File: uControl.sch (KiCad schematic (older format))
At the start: 4 parts

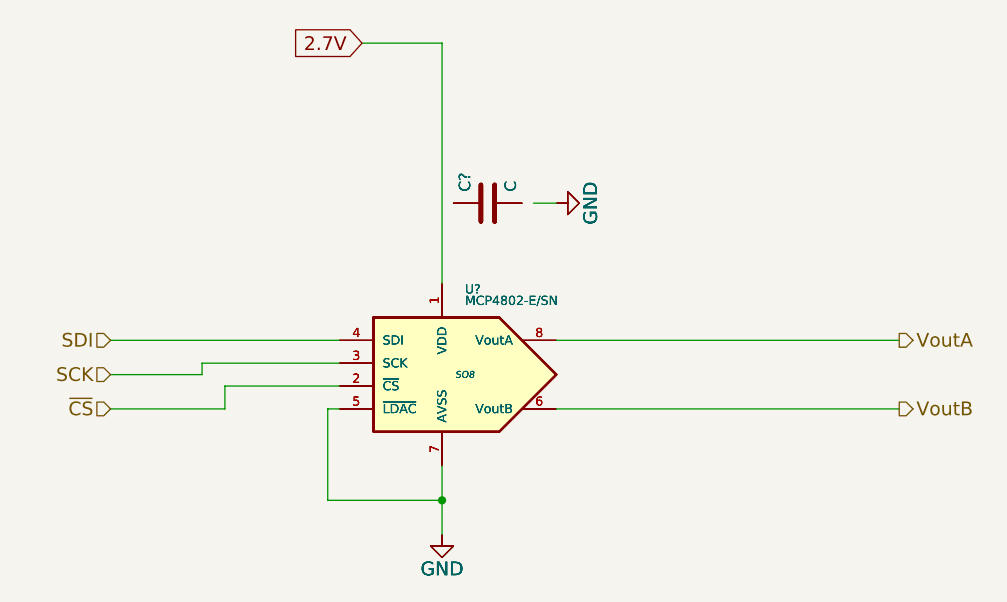
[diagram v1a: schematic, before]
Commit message: added additional regulator to power the ACS711 and potentially a micro at 3.3V
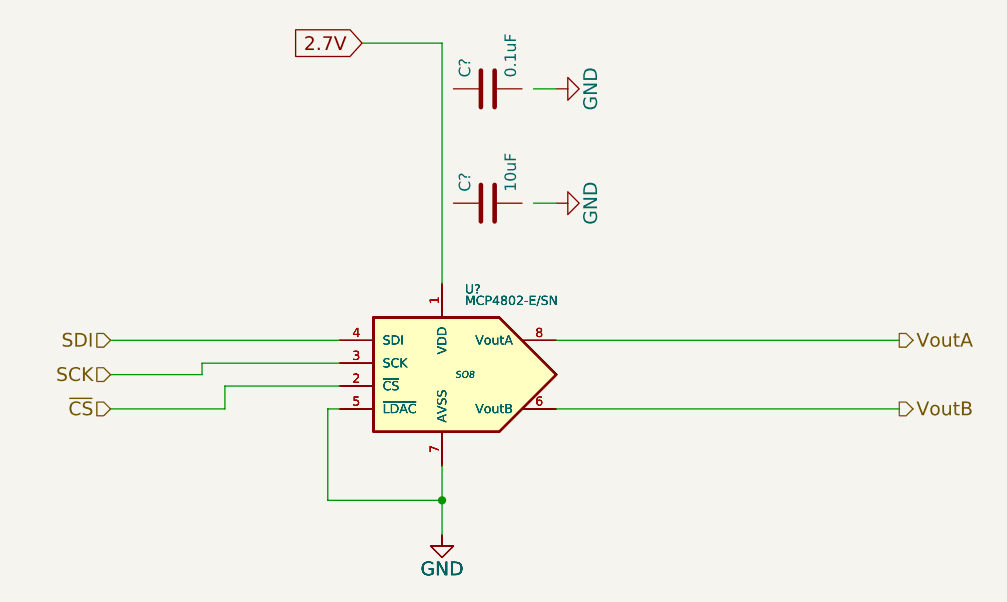
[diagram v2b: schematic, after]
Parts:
- removed C?: C, symbol C
- added C?: 0.1uF, symbol C
- C?: value C -> 10uF; MPN (none) -> Value
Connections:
- wire segments 16 -> 17
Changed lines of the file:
@@
-$EndComp
-$Comp
-L C C?
-U 1 1 55219CBF
-P 5750 3600
-F 0 "C?" H 5800 3700 50  0000 L CNN
-F 1 "C" H 5800 3500 50  0000 L CNN
-F 2 "" H 5788 3450 30  0000 C CNN
-F 3 "" H 5750 3600 60  0000 C CNN
-	1    5750 3600
-	0    -1   -1   0
-$EndComp
-$Comp
-L GND #PWR?
-U 1 1 55219CC6
-P 6050 3600
-F 0 "#PWR?" H 6050 3350 60  0001 C CNN
-F 1 "GND" H 6050 3450 60  0000 C CNN
-F 2 "" H 6050 3600 60  0000 C CNN
-F 3 "" H 6050 3600 60  0000 C CNN
-	1    6050 3600
-	0    -1   -1   0
 $EndComp
 $Comp
@@
 P 5750 3600
 F 0 "C?" H 5800 3700 50  0000 L CNN
-F 1 "C" H 5800 3500 50  0000 L CNN
+F 1 "10uF" H 5800 3500 50  0000 L CNN
 F 2 "" H 5788 3450 30  0000 C CNN
 F 3 "" H 5750 3600 60  0000 C CNN
+F 4 "Value" H 5750 3600 60  0001 C CNN "MPN"
 	1    5750 3600
 	0    -1   -1   0
@@
 Wire Wire Line
 	5100 4200 4100 4200
+$Comp
+L C C?
+U 1 1 5522A421
+P 5750 3100
+F 0 "C?" H 5800 3200 50  0000 L CNN
+F 1 "0.1uF" H 5800 3000 50  0000 L CNN
+F 2 "" H 5788 2950 30  0000 C CNN
+F 3 "" H 5750 3100 60  0000 C CNN
+	1    5750 3100
+	0    -1   -1   0
+$EndComp
+$Comp
+L GND #PWR?
+U 1 1 5522A47A
+P 6050 3100
+F 0 "#PWR?" H 6050 2850 60  0001 C CNN
+F 1 "GND" H 6050 2950 60  0000 C CNN
+F 2 "" H 6050 3100 60  0000 C CNN
+F 3 "" H 6050 3100 60  0000 C CNN
+	1    6050 3100
+	0    -1   -1   0
+$EndComp
+Wire Wire Line
+	5950 3100 6050 3100
 $EndSCHEMATC

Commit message: updated with association labels
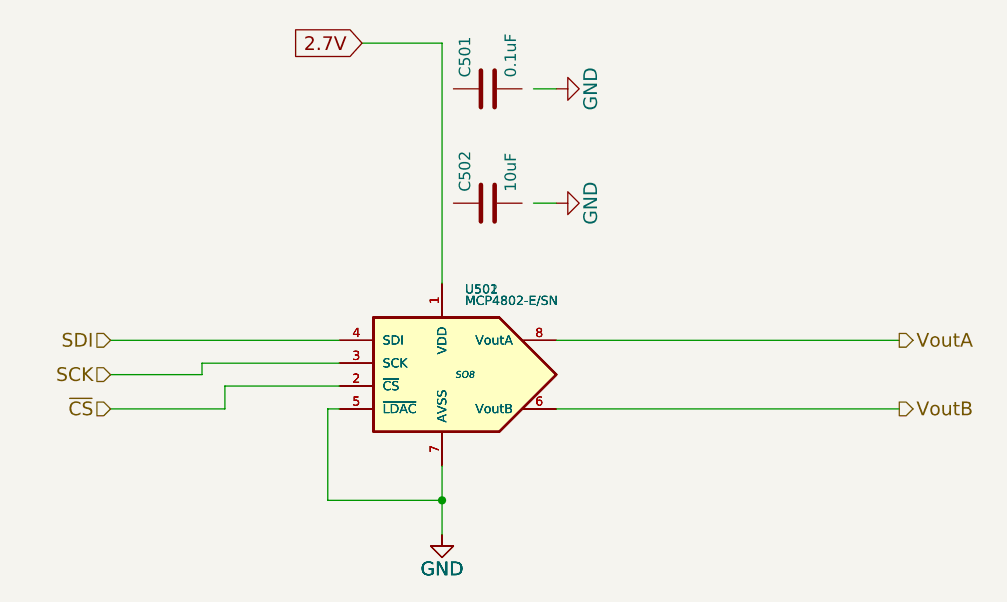
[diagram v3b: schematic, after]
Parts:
- gave numbers to parts that had none: 4
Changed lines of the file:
@@
 $EndDescr
 $Comp
-L GND #PWR?
+L GND #PWR501
 U 1 1 55219CB2
 P 5550 5050
-F 0 "#PWR?" H 5550 4800 60  0001 C CNN
+F 0 "#PWR501" H 5550 4800 60  0001 C CNN
 F 1 "GND" H 5550 4900 60  0000 C CNN
 F 2 "" H 5550 5050 60  0000 C CNN
@@
 $EndComp
 $Comp
-L MCP4802-E/SN U?
+L MCP4802-E/SN U501
 U 1 1 55219CB8
 P 5650 4350
-F 0 "U?" H 5650 4700 40  0000 L BNN
+F 0 "U501" H 5650 4700 40  0000 L BNN
 F 1 "MCP4802-E/SN" H 5650 4650 40  0000 L BNN
 F 2 "SO8" H 5650 4350 30  0000 C CIN
@@
 $EndComp
 $Comp
-L GND #PWR?
+L GND #PWR502
 U 1 1 55219CCC
 P 5550 5050
-F 0 "#PWR?" H 5550 4800 60  0001 C CNN
+F 0 "#PWR502" H 5550 4800 60  0001 C CNN
 F 1 "GND" H 5550 4900 60  0000 C CNN
 F 2 "" H 5550 5050 60  0000 C CNN
@@
 $EndComp
 $Comp
-L MCP4802-E/SN U?
+L MCP4802-E/SN U502
 U 1 1 55219CD2
 P 5650 4350
-F 0 "U?" H 5650 4700 40  0000 L BNN
+F 0 "U502" H 5650 4700 40  0000 L BNN
 F 1 "MCP4802-E/SN" H 5650 4650 40  0000 L BNN
 F 2 "SO8" H 5650 4350 30  0000 C CIN
@@
 $EndComp
 $Comp
-L C C?
+L C C502
 U 1 1 55219CD9
 P 5750 3600
-F 0 "C?" H 5800 3700 50  0000 L CNN
+F 0 "C502" H 5800 3700 50  0000 L CNN
 F 1 "10uF" H 5800 3500 50  0000 L CNN
 F 2 "" H 5788 3450 30  0000 C CNN
@@
 $EndComp
 $Comp
-L GND #PWR?
+L GND #PWR504
 U 1 1 55219CE0
 P 6050 3600
-F 0 "#PWR?" H 6050 3350 60  0001 C CNN
+F 0 "#PWR504" H 6050 3350 60  0001 C CNN
 F 1 "GND" H 6050 3450 60  0000 C CNN
 F 2 "" H 6050 3600 60  0000 C CNN
@@
 	5100 4200 4100 4200
 $Comp
-L C C?
+L C C501
 U 1 1 5522A421
 P 5750 3100
-F 0 "C?" H 5800 3200 50  0000 L CNN
+F 0 "C501" H 5800 3200 50  0000 L CNN
 F 1 "0.1uF" H 5800 3000 50  0000 L CNN
 F 2 "" H 5788 2950 30  0000 C CNN
@@
 $EndComp
 $Comp
-L GND #PWR?
+L GND #PWR503
 U 1 1 5522A47A
 P 6050 3100
-F 0 "#PWR?" H 6050 2850 60  0001 C CNN
+F 0 "#PWR503" H 6050 2850 60  0001 C CNN
 F 1 "GND" H 6050 2950 60  0000 C CNN
 F 2 "" H 6050 3100 60  0000 C CNN

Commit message: updated schematic with corrected wiring after all passives became disconnected
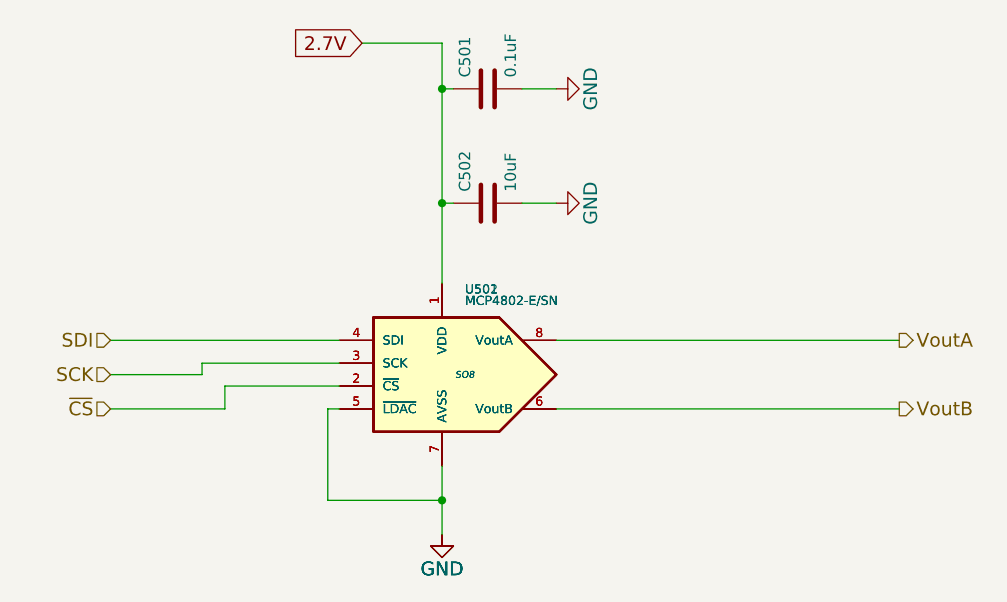
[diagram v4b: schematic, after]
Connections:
- wire segments 17 -> 19
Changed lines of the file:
@@
 	5050 4900 5550 4900
 Wire Wire Line
-	5950 3600 6050 3600
+	5900 3600 6050 3600
 Wire Wire Line
 	6050 4500 7550 4500
@@
 $EndComp
 Wire Wire Line
-	5950 3100 6050 3100
+	5900 3100 6050 3100
+Wire Wire Line
+	5600 3600 5550 3600
+Connection ~ 5550 3600
+Wire Wire Line
+	5600 3100 5550 3100
+Connection ~ 5550 3100
 $EndSCHEMATC

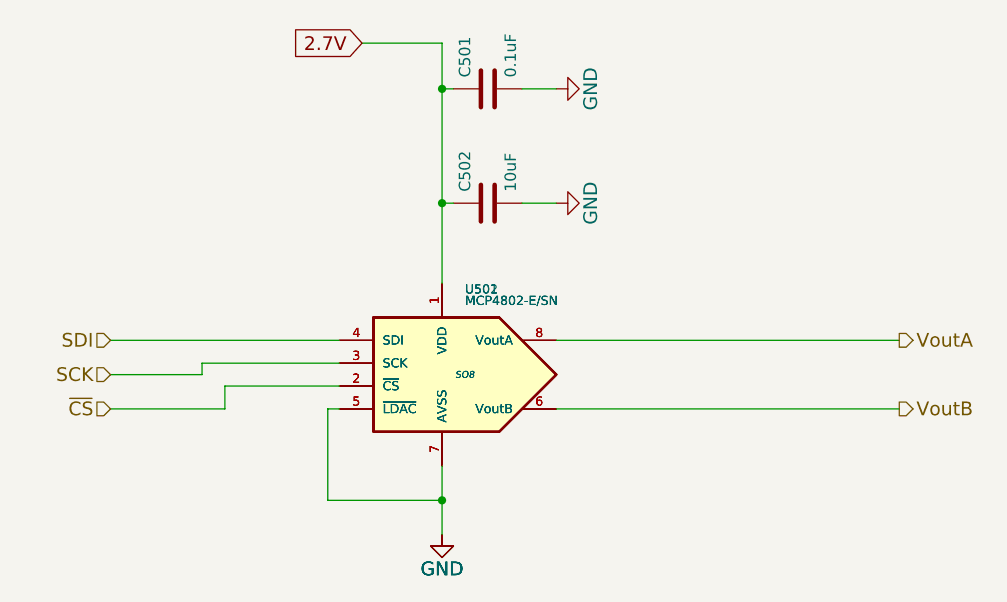
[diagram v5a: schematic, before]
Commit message: updated project with most footprint associations
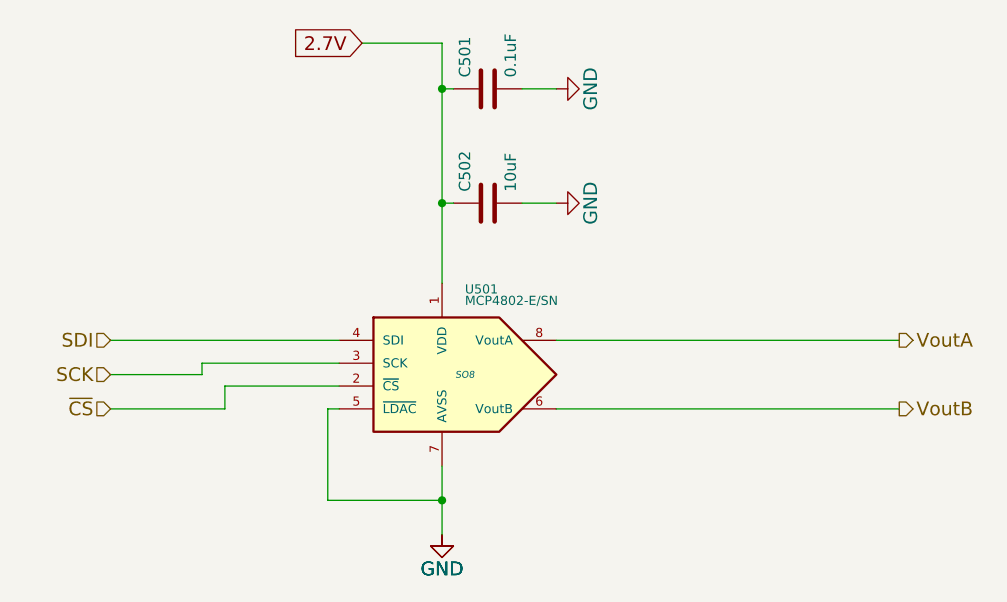
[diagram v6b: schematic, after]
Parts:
- removed U502: MCP4802-E/SN, SO8, symbol MCP4802-E/SN
- C501, C502: footprint (none) -> Capacitors_SMD:C_0805_HandSoldering
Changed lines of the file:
@@
 $EndDescr
 $Comp
-L GND #PWR024
+L GND #PWR501
 U 1 1 55219CB2
 P 5550 5050
-F 0 "#PWR024" H 5550 4800 60  0001 C CNN
+F 0 "#PWR501" H 5550 4800 60  0001 C CNN
 F 1 "GND" H 5550 4900 60  0000 C CNN
 F 2 "" H 5550 5050 60  0000 C CNN
@@
 $EndComp
 $Comp
-L GND #PWR025
+L GND #PWR502
 U 1 1 55219CCC
 P 5550 5050
-F 0 "#PWR025" H 5550 4800 60  0001 C CNN
+F 0 "#PWR502" H 5550 4800 60  0001 C CNN
 F 1 "GND" H 5550 4900 60  0000 C CNN
 F 2 "" H 5550 5050 60  0000 C CNN
 F 3 "" H 5550 5050 60  0000 C CNN
 	1    5550 5050
-	1    0    0    -1
-$EndComp
-$Comp
-L MCP4802-E/SN U502
-U 1 1 55219CD2
-P 5650 4350
-F 0 "U502" H 5650 4700 40  0000 L BNN
-F 1 "MCP4802-E/SN" H 5650 4650 40  0000 L BNN
-F 2 "SO8" H 5650 4350 30  0000 C CIN
-F 3 "" H 5650 4350 60  0000 C CNN
-	1    5650 4350
 	1    0    0    -1
 $EndComp
@@
 F 0 "C502" H 5800 3700 50  0000 L CNN
 F 1 "10uF" H 5800 3500 50  0000 L CNN
-F 2 "" H 5788 3450 30  0000 C CNN
+F 2 "Capacitors_SMD:C_0805_HandSoldering" H 5788 3450 30  0001 C CNN
 F 3 "" H 5750 3600 60  0000 C CNN
 F 4 "Value" H 5750 3600 60  0001 C CNN "MPN"
@@
 $EndComp
 $Comp
-L GND #PWR026
+L GND #PWR504
 U 1 1 55219CE0
 P 6050 3600
-F 0 "#PWR026" H 6050 3350 60  0001 C CNN
+F 0 "#PWR504" H 6050 3350 60  0001 C CNN
 F 1 "GND" H 6050 3450 60  0000 C CNN
 F 2 "" H 6050 3600 60  0000 C CNN
@@
 F 0 "C501" H 5800 3200 50  0000 L CNN
 F 1 "0.1uF" H 5800 3000 50  0000 L CNN
-F 2 "" H 5788 2950 30  0000 C CNN
+F 2 "Capacitors_SMD:C_0805_HandSoldering" H 5788 2950 30  0001 C CNN
 F 3 "" H 5750 3100 60  0000 C CNN
 	1    5750 3100
@@
 $EndComp
 $Comp
-L GND #PWR027
+L GND #PWR503
 U 1 1 5522A47A
 P 6050 3100
-F 0 "#PWR027" H 6050 2850 60  0001 C CNN
+F 0 "#PWR503" H 6050 2850 60  0001 C CNN
 F 1 "GND" H 6050 2950 60  0000 C CNN
 F 2 "" H 6050 3100 60  0000 C CNN

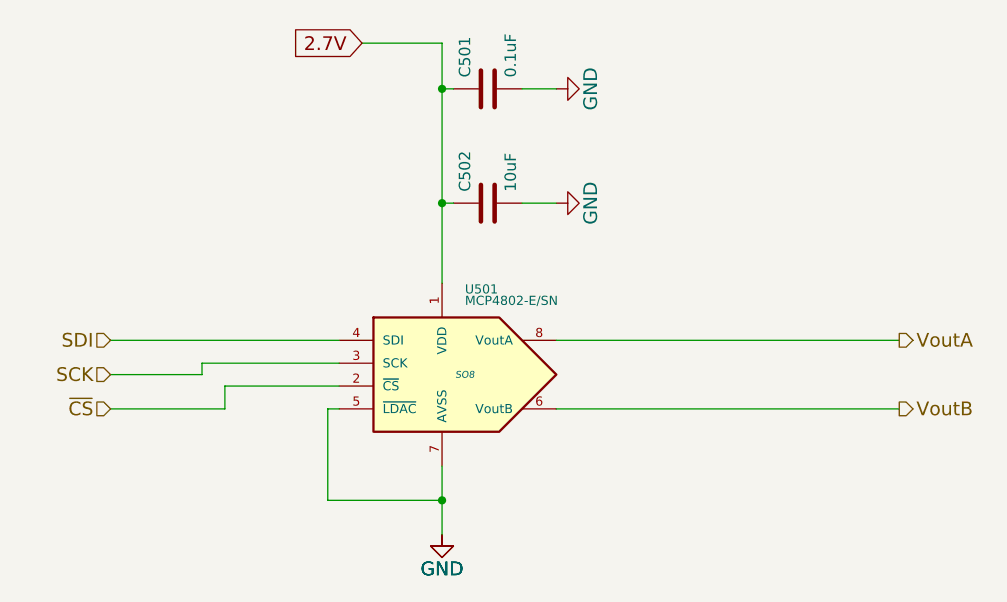
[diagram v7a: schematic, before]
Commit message: removed duplicates and bad wire connections to enable the generation of a PCB
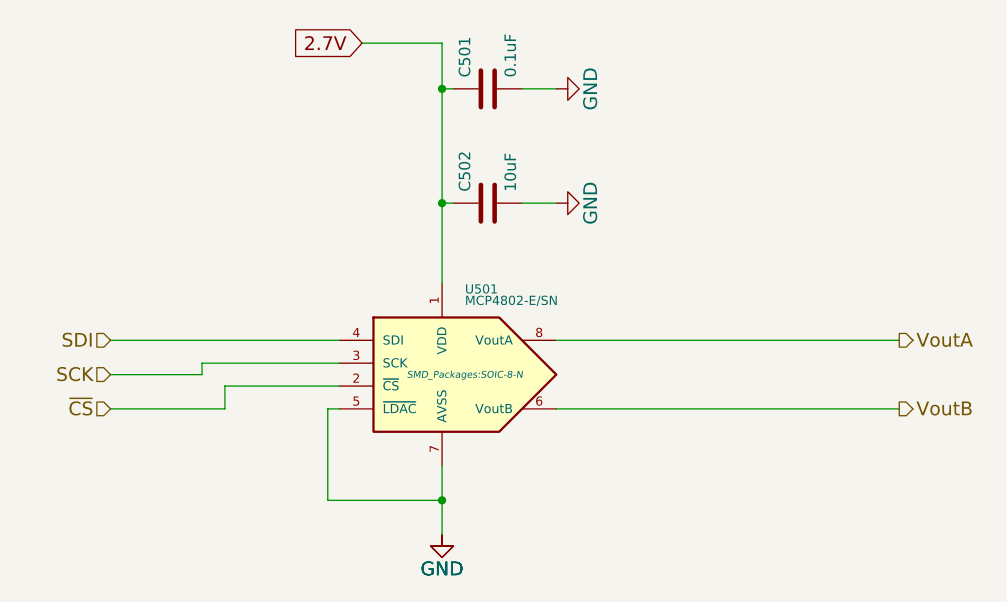
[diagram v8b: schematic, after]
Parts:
- U501: footprint SO8 -> SMD_Packages:SOIC-8-N
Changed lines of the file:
@@
 F 0 "U501" H 5650 4700 40  0000 L BNN
 F 1 "MCP4802-E/SN" H 5650 4650 40  0000 L BNN
-F 2 "SO8" H 5650 4350 30  0000 C CIN
+F 2 "SMD_Packages:SOIC-8-N" H 5650 4350 30  0000 C CIN
 F 3 "" H 5650 4350 60  0000 C CNN
 	1    5650 4350
